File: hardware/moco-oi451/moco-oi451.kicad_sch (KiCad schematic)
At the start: 0 parts

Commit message: OI451 routed
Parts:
- added C1, C2: 1uF, Capacitor_SMD:C_0603_1608Metric, symbol Device:C
- added H1, H2, H3: MountingHole, MountingHole:MountingHole_2.2mm_M2_ISO14580, symbol Mechanical:MountingHole
- added J1: V+, moco:wire_3.2mm, symbol Connector_Generic:Conn_01x01
- added J2: V-, moco:wire_3.2mm, symbol Connector_Generic:Conn_01x01
- added J3, J4: Serial, Connector_JST:JST_GH_SM03B-GHS-TB_1x03-1MP_P1.25mm_Horizontal, symbol Connector_Generic:Conn_01x03
- added J5: Debug, Connector_PinHeader_2.54mm:PinHeader_2x04_P2.54mm_Vertical, symbol Connector_Generic:Conn_02x04_Odd_Even
- added LD1: LED_BAGR, moco:RGB LED 1.6x1.6mm, symbol Device:LED_BAGR
- added NT?: NetTie_2, NetTie:NetTie-2_SMD_Pad0.5mm, symbol Device:NetTie_2
- added R2, R4: 1k, Resistor_SMD:R_0402_1005Metric, symbol Device:R
- added R3: 5k, Resistor_SMD:R_0402_1005Metric, symbol Device:R
- added SB1: SolderJumper_2_Open, Jumper:SolderJumper-2_P1.3mm_Open_RoundedPad1.0x1.5mm, symbol Jumper:SolderJumper_2_Open
- added TP1: V_{CC}, TestPoint:TestPoint_Pad_D1.0mm, symbol Connector:TestPoint
- added U1: RT9013-33GB, Package_TO_SOT_SMD:SOT-23-5, symbol rp-micro:RT9013-33GB
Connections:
- new net: LD1.3 (GK), R3.1
- new net: LD1.1 (BK), R4.1
- new net: LD1.4 (RK), R2.1
- new net +3.3V: C2.1, J5.1 (Pin_1), SB1.2 (B), TP1.1, U1.5 (VOUT)
- new net +5V: C1.1, J5.2 (Pin_2), LD1.2 (A), SB1.1 (A), U1.1 (VIN), U1.3 (EN)
- new net GND: C1.2, C2.2, J3.3 (Pin_3), J4.3 (Pin_3), J5.7 (Pin_7), J5.8 (Pin_8), NT?.2, R3.2, U1.2 (GND)
- new net GNDPWR: J2.1 (Pin_1), NT?.1
- new net SWCLK: J5.4 (Pin_4)
- new net SWDIO: J5.6 (Pin_6)
- new net UART1_RX: J3.2 (Pin_2), J5.3 (Pin_3)
- new net UART1_TX: J3.1 (Pin_1), J5.5 (Pin_5)
- new net UART2_RX: J4.2 (Pin_2)
- new net UART2_TX: J4.1 (Pin_1)
- new net USER_LED1: R2.2
- new net USER_LED2: R4.2
- new net Vdrive: J1.1 (Pin_1)
- no-connect marks 0 -> 6
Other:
- added sheet  Rotary Sensor (rotary_sensor.kicad_sch)
- added sheet Driver (driver.kicad_sch)
- added sheet MCU (mcu.kicad_sch)
- note added: "LDO"
- note added: "LED"
- note added: "LED Forward Voltage (V_{F}): R: 1.9~2.2V G: 2.9~3.4V B: 2.9~3.4V"

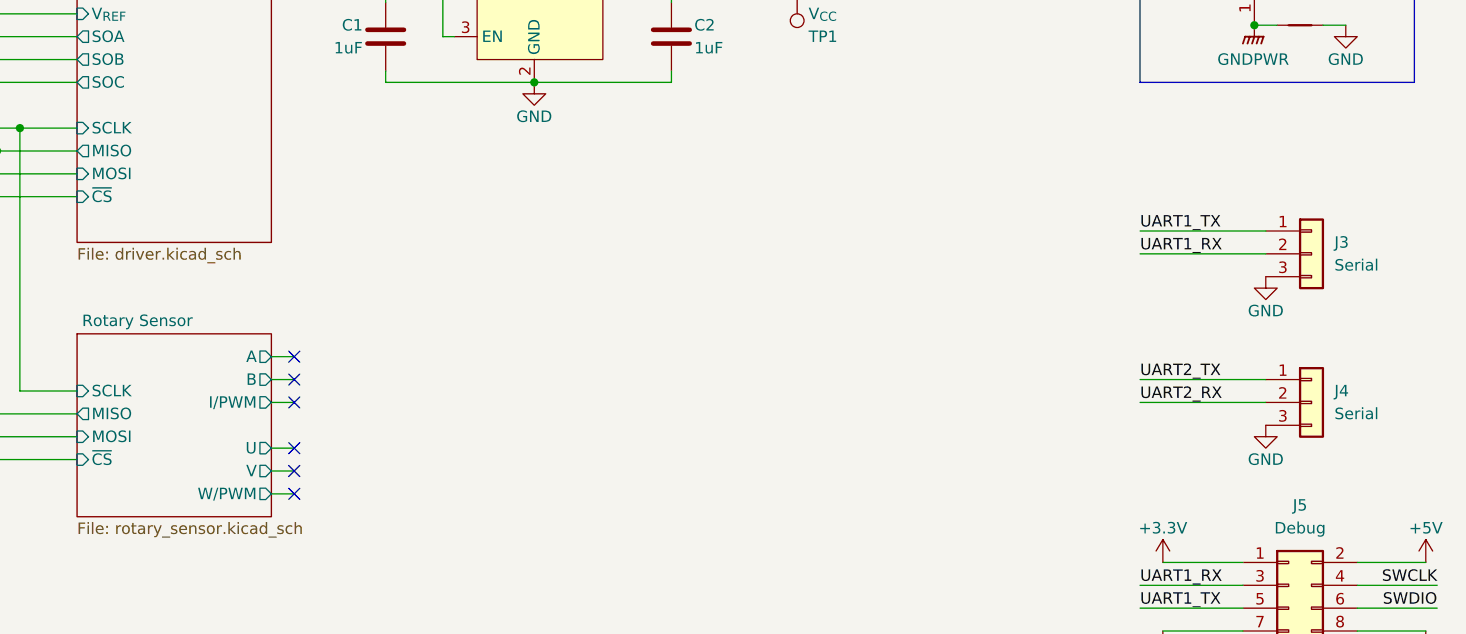
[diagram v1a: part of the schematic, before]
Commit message: Reroute and reduce size to Ø40mm
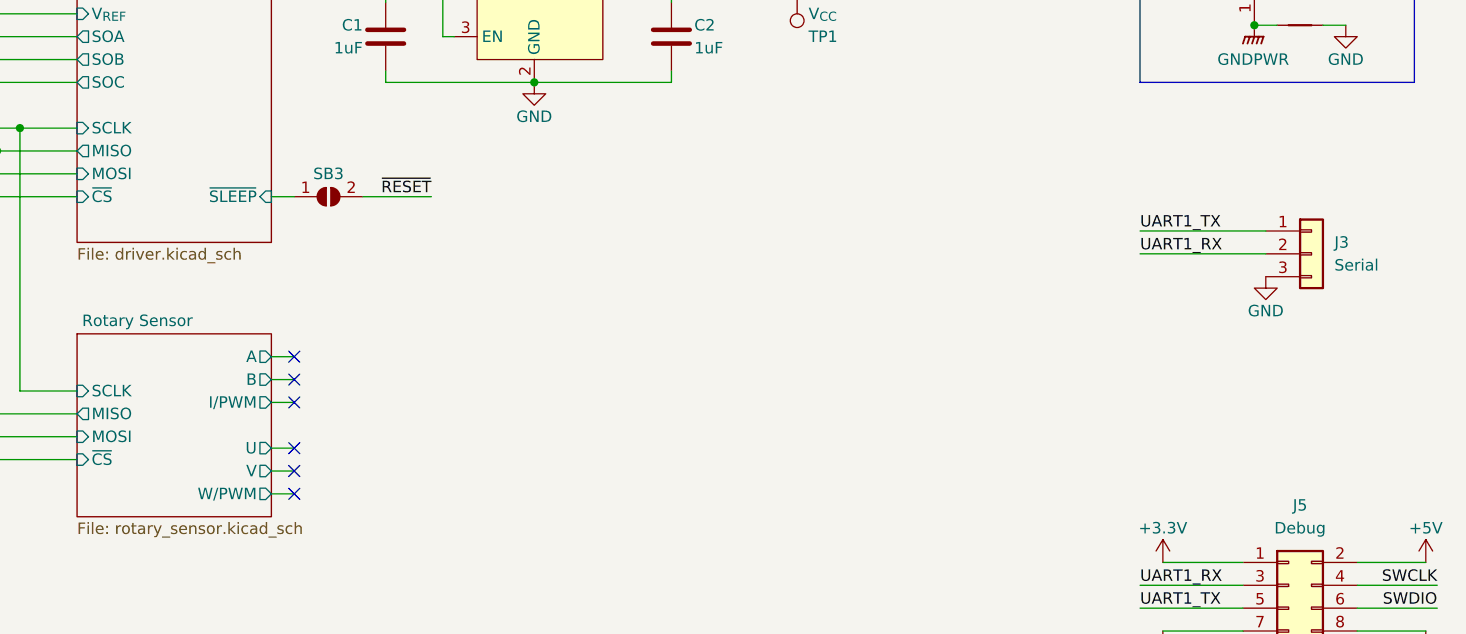
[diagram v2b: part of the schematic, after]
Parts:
- removed J4: Serial, Connector_JST:JST_GH_SM03B-GHS-TB_1x03-1MP_P1.25mm_Horizontal, symbol Connector_Generic:Conn_01x03
- added SB3: SolderJumper_2_Open, Jumper:SolderJumper-2_P1.3mm_Open_RoundedPad1.0x1.5mm, symbol Jumper:SolderJumper_2_Open
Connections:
- net ~{RESET}: now also SB3.2 (B)
- new net Driver/~{SLEEP}: SB3.1 (A)
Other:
- sheet Driver ports: added ~{SLEEP}; removed none
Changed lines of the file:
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@@
+    (stroke (width 0) (type default))
+  )
+  (wire (pts (xy 158.75 88.9) (xy 151.13 88.9))
     (stroke (width 0) (type default))
   )
@@
     (stroke (width 0) (type default))
   )
-  (wire (pts (xy 237.49 111.76) (xy 251.46 111.76))
-    (stroke (width 0) (type default))
-  )
   (wire (pts (xy 41.91 43.18) (xy 52.07 43.18))
     (stroke (width 0) (type default))
@@
     (stroke (width 0) (type default))
   )
+  (wire (pts (xy 140.97 88.9) (xy 143.51 88.9))
+    (stroke (width 0) (type default))
+  )
   (wire (pts (xy 240.03 129.54) (xy 248.92 129.54))
     (stroke (width 0) (type default))
@@
   )
   (wire (pts (xy 161.29 71.12) (xy 160.02 71.12))
-    (stroke (width 0) (type default))
-  )
-  (wire (pts (xy 237.49 109.22) (xy 251.46 109.22))
     (stroke (width 0) (type default))
   )
@@
     (effects (font (size 1.27 1.27)) (justify left bottom))
   )
-  (label "UART2_RX" (at 237.49 111.76 0) (fields_autoplaced)
-    (effects (font (size 1.27 1.27)) (justify left bottom))
+  (label "~{RESET}" (at 158.75 88.9 180) (fields_autoplaced)
+    (effects (font (size 1.27 1.27)) (justify right bottom))
   )
   (label "USER_LED1" (at 33.02 184.15 0) (fields_autoplaced)
@@
   (label "SWCLK" (at 270.51 132.08 180) (fields_autoplaced)
     (effects (font (size 1.27 1.27)) (justify right bottom))
-  )
-  (label "UART2_TX" (at 237.49 109.22 0) (fields_autoplaced)
-    (effects (font (size 1.27 1.27)) (justify left bottom))
   )
   (label "UART1_TX" (at 237.49 134.62 0) (fields_autoplaced)
@@
     )
   )
-  (symbol (lib_id "Connector_Generic:Conn_01x03") (at 256.54 111.76 0) (unit 1)
-    (in_bom yes) (on_board yes) (dnp no) (fields_autoplaced)
-    (property "Reference" "J4" (at 259.08 110.49 0)
-      (effects (font (size 1.27 1.27)) (justify left))
-    )
-    (property "Value" "Serial" (at 259.08 113.03 0)
-      (effects (font (size 1.27 1.27)) (justify left))
-    )
-    (property "Footprint" "Connector_JST:JST_GH_SM03B-GHS-TB_1x03-1MP_P1.25mm_Horizontal" (at 256.54 111.76 0)
-      (effects (font (size 1.27 1.27)) hide)
-    )
-    (property "Datasheet" "~" (at 256.54 111.76 0)
-      (effects (font (size 1.27 1.27)) hide)
-    )
-    (pin "1")
-    (pin "2")
-    (pin "3")
-    (instances
-      (project "moco-oi451"
-        (path "/171831cd-2a0d-47b9-8420-65898c688d08"
-          (reference "J4") (unit 1)
-        )
-      )
-      (project "moco-od501"
-        (path "/6af178d2-5089-4f26-a9dd-467044aa844a"
-          (reference "J?") (unit 1)
-        )
-      )
-    )
-  )
-  (symbol (lib_id "power:GND") (at 251.46 114.3 0) (unit 1)
-    (in_bom yes) (on_board yes) (dnp no)
-    (property "Reference" "#PWR08" (at 251.46 120.65 0)
-      (effects (font (size 1.27 1.27)) hide)
-    )
-    (property "Value" "GND" (at 251.46 118.11 0)
-      (effects (font (size 1.27 1.27)))
-    )
-    (property "Footprint" "" (at 251.46 114.3 0)
-      (effects (font (size 1.27 1.27)) hide)
-    )
-    (property "Datasheet" "" (at 251.46 114.3 0)
-      (effects (font (size 1.27 1.27)) hide)
-    )
-    (pin "1")
-    (instances
-      (project "moco-oi451"
-        (path "/171831cd-2a0d-47b9-8420-65898c688d08"
-          (reference "#PWR08") (unit 1)
-        )
-      )
-      (project "moco-od501"
-        (path "/6af178d2-5089-4f26-a9dd-467044aa844a"
-          (reference "#PWR?") (unit 1)
-        )
-      )
-    )
-  )
   (symbol (lib_id "Device:R") (at 50.8 186.69 270) (unit 1)
     (in_bom yes) (on_board yes) (dnp no)
@@
         (path "/6af178d2-5089-4f26-a9dd-467044aa844a"
           (reference "R?") (unit 1)
+        )
+      )
+    )
+  )
+  (symbol (lib_id "Jumper:SolderJumper_2_Open") (at 147.32 88.9 0) (unit 1)
+    (in_bom yes) (on_board yes) (dnp no)
+    (property "Reference" "SB3" (at 147.32 86.36 0)
+      (effects (font (size 1.27 1.27)))
+    )
+    (property "Value" "SolderJumper_2_Open" (at 147.32 85.09 0)
+      (effects (font (size 1.27 1.27)) hide)
+    )
+    (property "Footprint" "Jumper:SolderJumper-2_P1.3mm_Open_RoundedPad1.0x1.5mm" (at 147.32 88.9 0)
+      (effects (font (size 1.27 1.27)) hide)
+    )
+    (property "Datasheet" "~" (at 147.32 88.9 0)
+      (effects (font (size 1.27 1.27)) hide)
+    )
+    (pin "1")
+    (pin "2")
+    (instances
+      (project "moco-oi451"
+        (path "/171831cd-2a0d-47b9-8420-65898c688d08"
+          (reference "SB3") (unit 1)
+        )
+        (path "/171831cd-2a0d-47b9-8420-65898c688d08/e49edf63-a462-4dde-9ddc-a334d0522771"
+          (reference "SB?") (unit 1)
+        )
+      )
+      (project "moco-bkd8316"
+        (path "/60ff2a18-57fe-4fe9-a422-66a2356bfaaa"
+          (reference "SB?") (unit 1)
         )
       )
@@
       (effects (font (size 1.27 1.27)) (justify right))
     )
+    (pin "~{SLEEP}" input (at 140.97 88.9 0)
+      (effects (font (size 1.27 1.27)) (justify right))
+    )

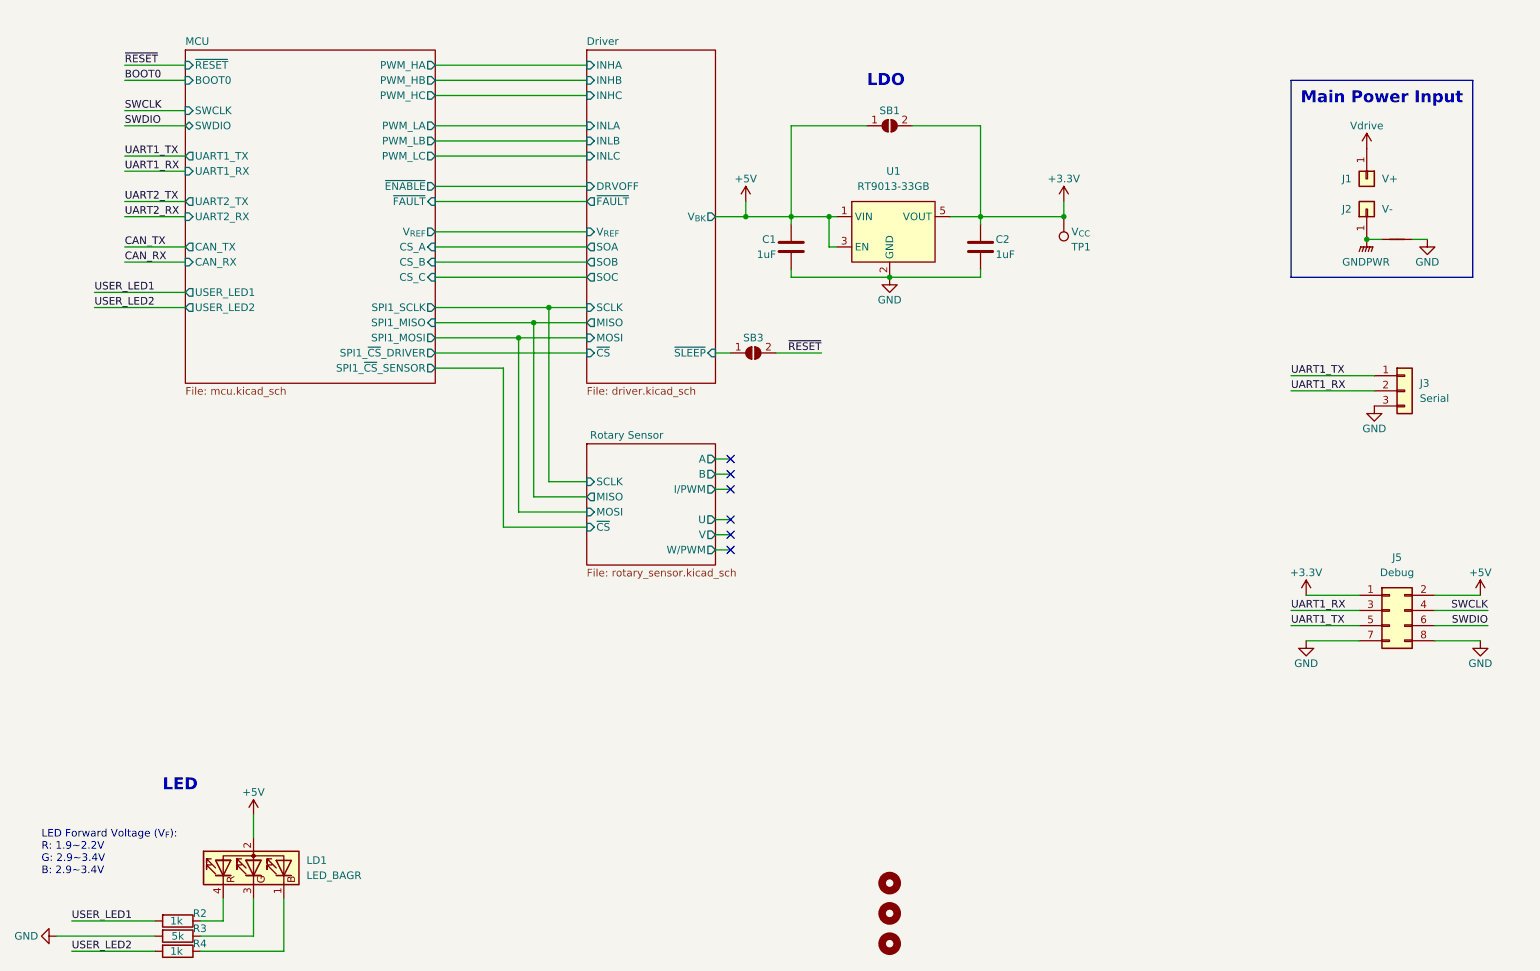
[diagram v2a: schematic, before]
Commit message: Optimize routing
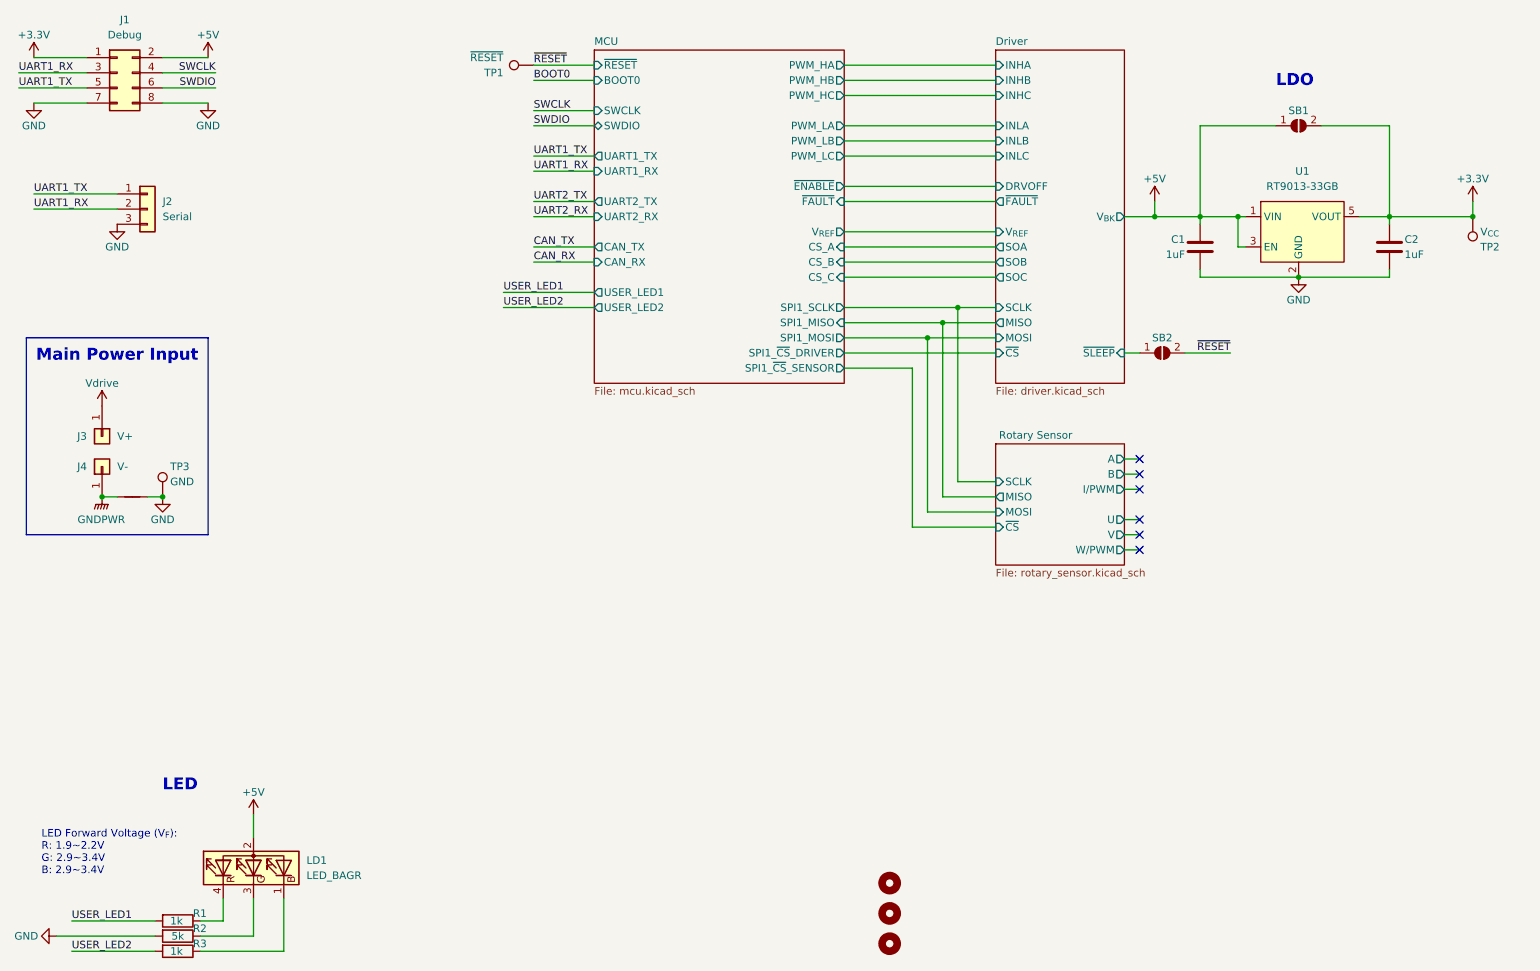
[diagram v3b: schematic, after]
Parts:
- added TP1: ~{RESET}, TestPoint:TestPoint_Pad_D1.0mm, symbol Connector:TestPoint
- added TP3: GND, TestPoint:TestPoint_Pad_D1.0mm, symbol Connector:TestPoint
- renumbered J5 to J1, J3 to J2, J1 to J3, J2 to J4, R2 to R1, R3 to R2, R4 to R3, SB3 to SB2, TP1 to TP2
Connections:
- net GND: now also TP3.1
- net ~{RESET}: now also TP1.1
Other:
- moved on the sheet: C1, C2, J1, J2, J3, J4, SB1, SB2, TP2, U1
